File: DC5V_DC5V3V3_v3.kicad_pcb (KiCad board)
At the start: 2 copper layers, 24 parts, among them J1 Vout1, J2 Vout2, Q1 BSS138, U1 LM1117-3.3

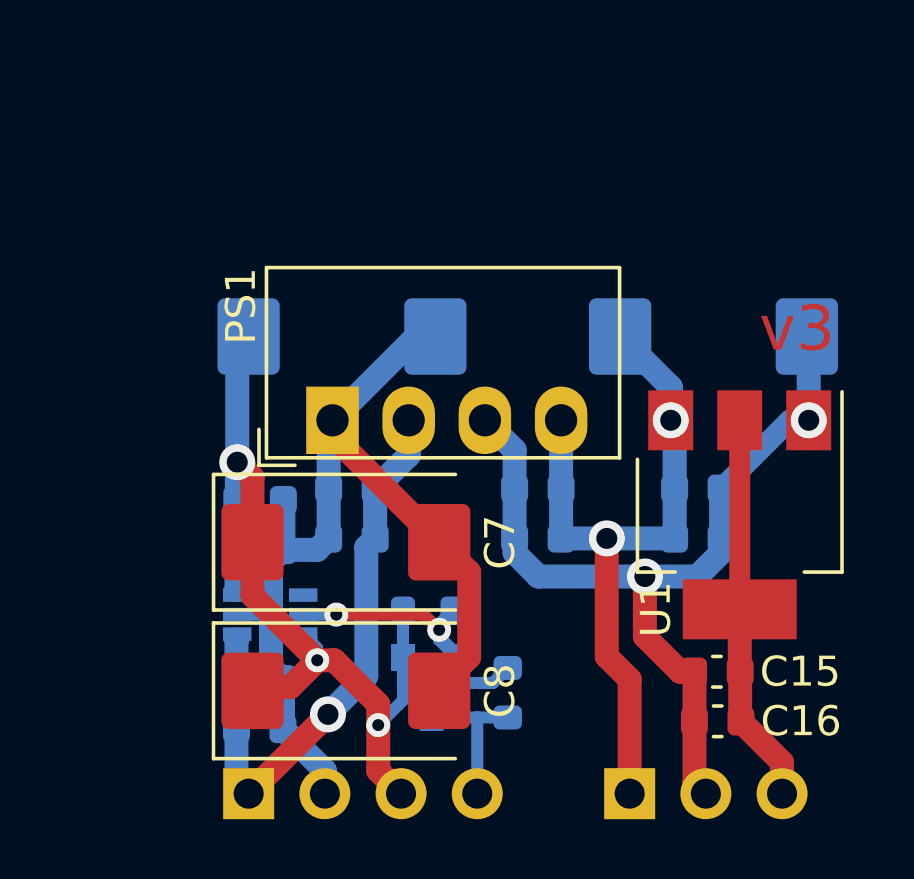
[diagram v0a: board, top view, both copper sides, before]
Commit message: Сформирован перечень элементов, 3D-модель, исправлены ошибки, реализована панелизация платы.
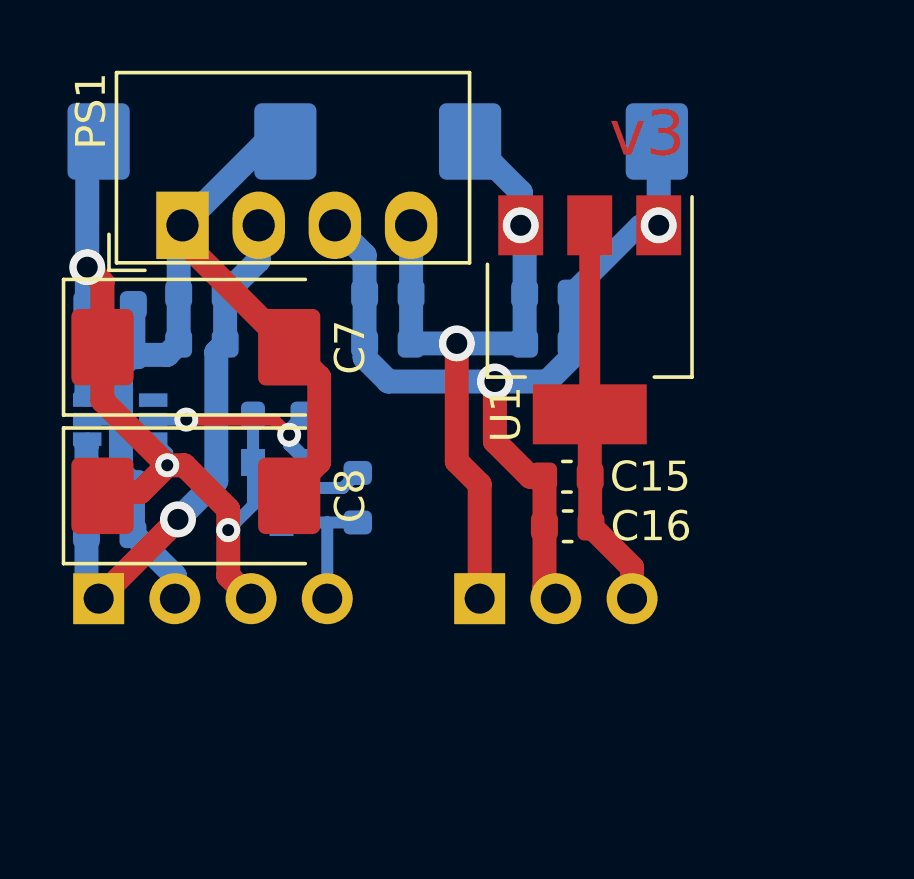
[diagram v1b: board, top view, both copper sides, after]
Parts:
- J1: footprint Modules:PinHeader_1x04_P2.54mm_Horizontal -> Modules:PinHeader_1x04_P2.54mm_Horizontal_short
- J2: footprint Modules:PinHeader_1x03_P2.54mm_Horizontal -> Modules:PinHeader_1x03_P2.54mm_Horizontal_short
- moved C1 8.20 mm to (87.0, 89.9)
- moved C10 8.20 mm to (96.2, 83.6)
- moved C11 8.20 mm to (89.7, 76.9)
- moved C12 8.20 mm to (102.1, 76.9)
- moved C13 8.20 mm to (101.6, 81.9)
- moved C14 8.20 mm to (101.6, 83.6)
- moved C15 8.20 mm to (102.2, 88.0)
- moved C16 8.20 mm to (102.2, 89.7)
- moved C2 8.20 mm to (90.0, 83.6)
- moved C3 8.20 mm to (87.0, 88.3)
- moved C4 8.20 mm to (90.0, 81.9)
- moved C5 8.20 mm to (87.0, 84.0)
- moved C6 8.20 mm to (87.0, 82.3)
- moved C7 8.20 mm to (89.8, 83.7)
- moved C8 8.20 mm to (89.8, 88.7)
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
